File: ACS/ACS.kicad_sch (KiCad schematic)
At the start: 9 parts, among them J1 Screw_Terminal_01x02, Q1 IRLB8721PBF, U1 Teensy4.1

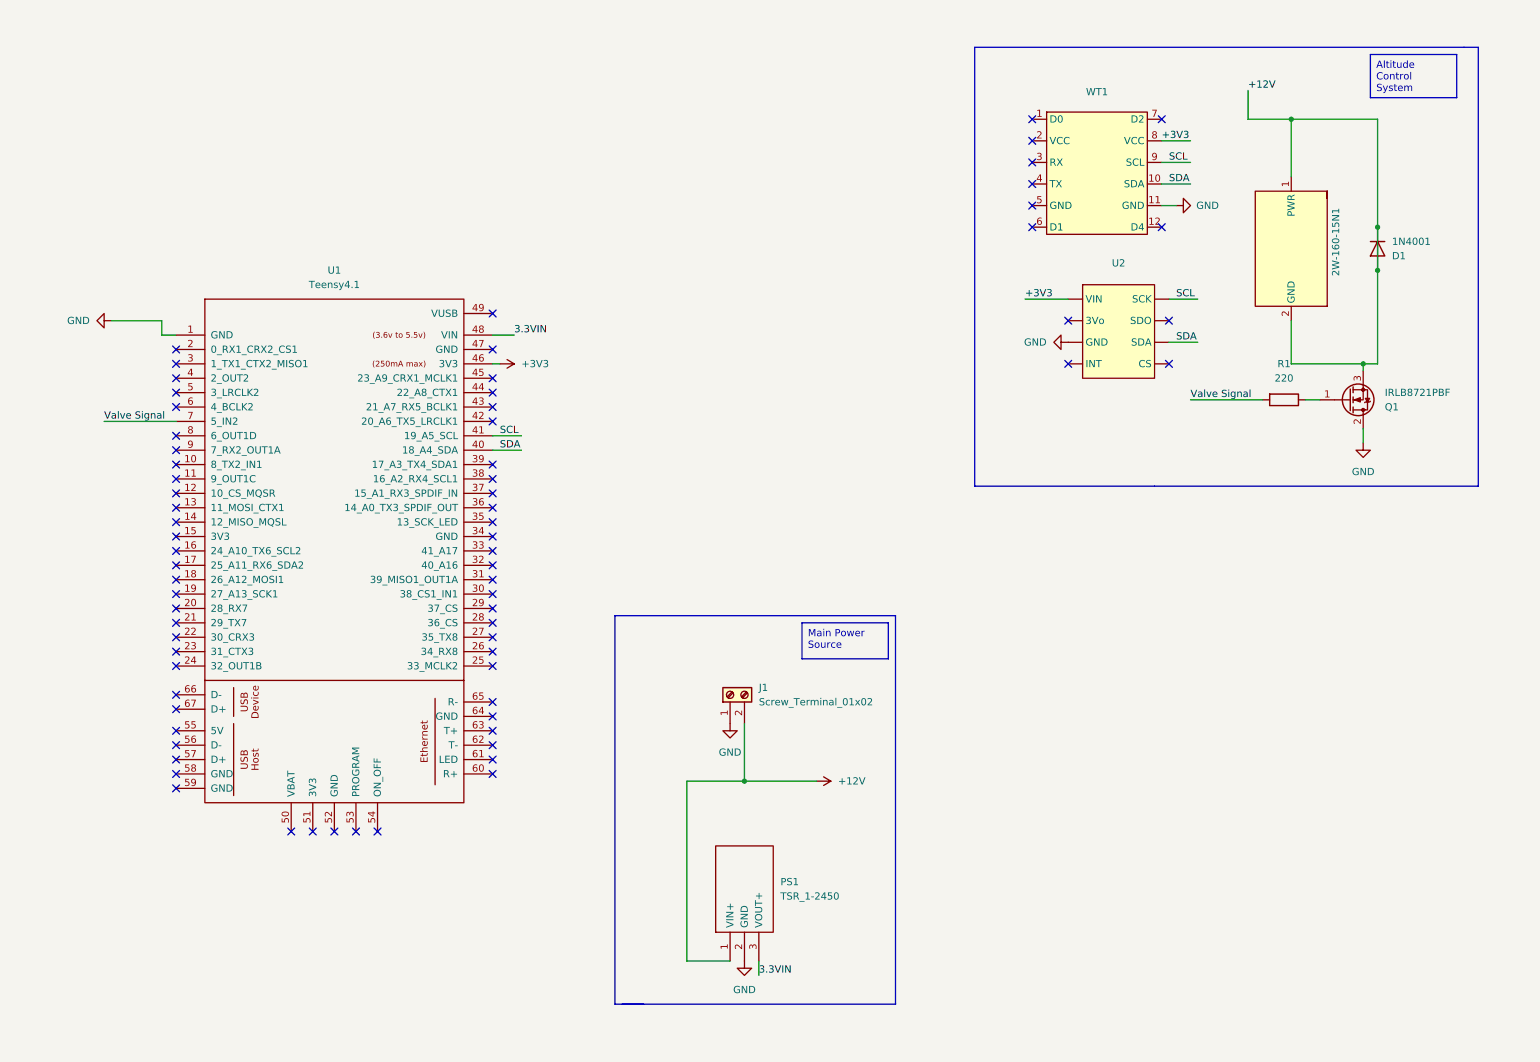
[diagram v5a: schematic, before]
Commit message: Add Switch and Heating Pad
Added wiring for switch and heating pad for ACS. Fix wiring schematic IRLB8721 for solenoid control
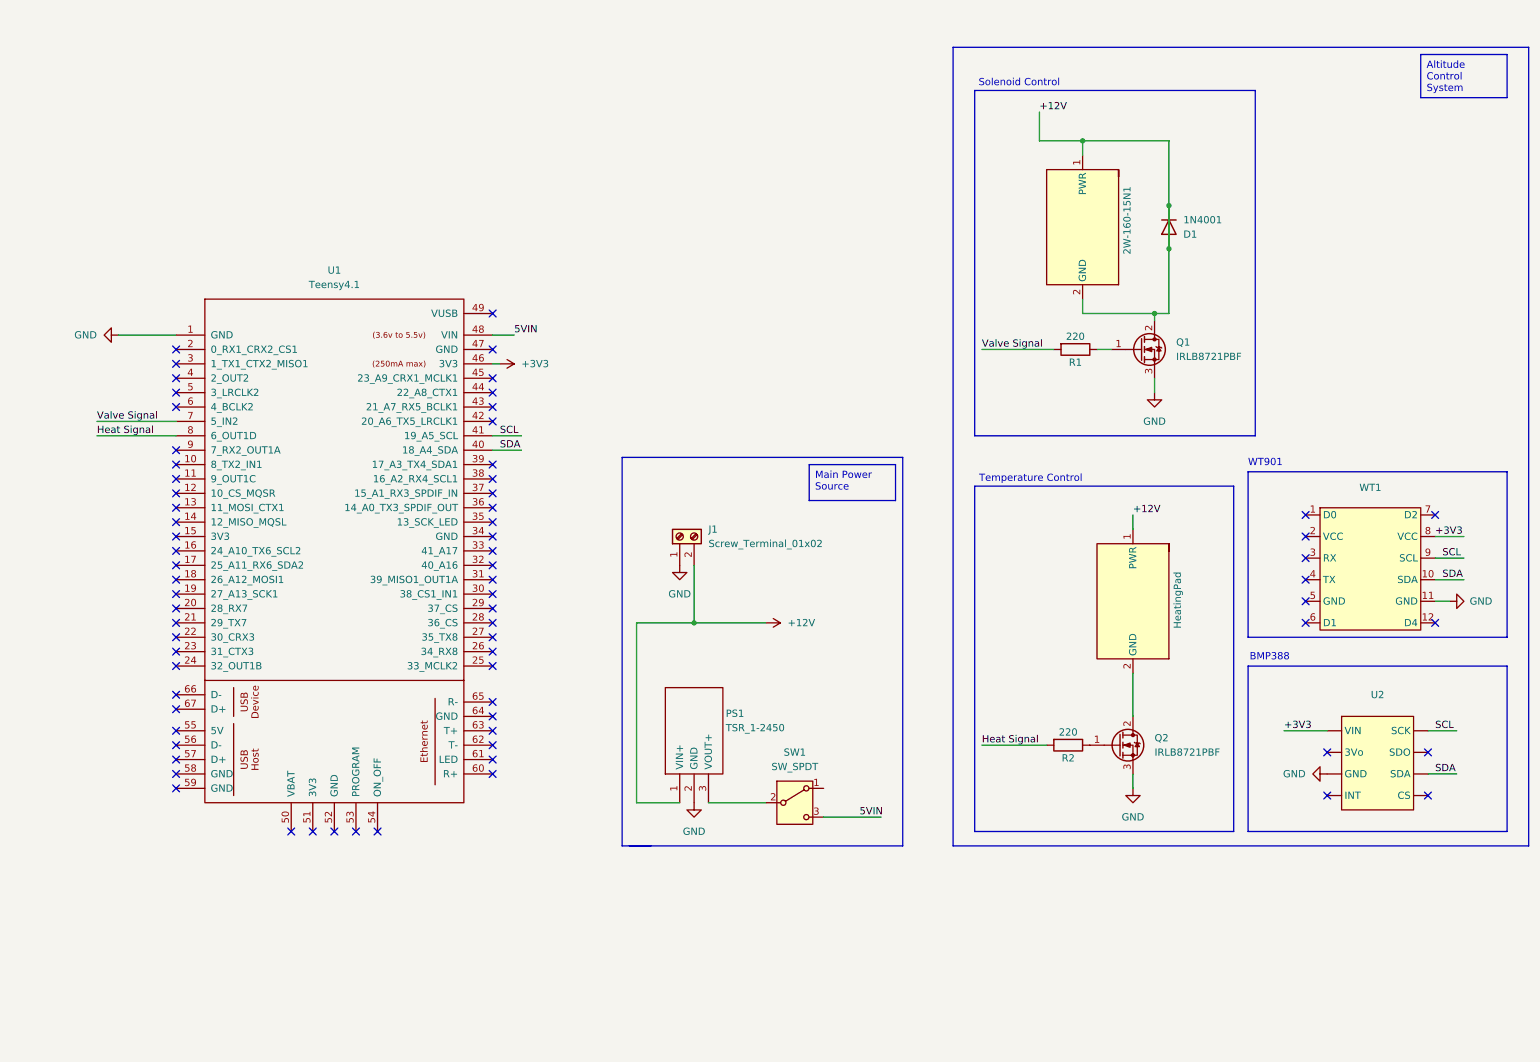
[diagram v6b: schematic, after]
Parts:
- added HeatingPad: ~, TerminalBlock_RND:TerminalBlock_RND_205-00276_1x02_P5.00mm_Vertical, symbol GRS_Valve:2W-160-15
- added Q2: IRLB8721PBF, Package_TO_SOT_THT:TO-220-3_Vertical, symbol Transistor_FET:IRLB8721PBF
- added R2: 220, symbol Device:R
- added SW1: SW_SPDT, symbol Switch:SW_SPDT
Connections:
- net +12V: now also Q1.2 (D), HeatingPad.1 (PWR); no longer Q1.3 (S)
- net GND: now also Q1.3 (S), Q2.3 (S); no longer Q1.2 (D)
- net Heat Signal: now reaches U1.8 (6_OUT1D)
- net Heat Signal: now also R2.2
- net 3.3VIN: no longer names the net of PS1.3 (VOUT+)
- net 3.3VIN: now also SW1.2 (B); no longer U1.48 (VIN)
- new net: HeatingPad.2 (GND), Q2.2 (D)
- new net: Q2.1 (G), R2.1
- new net 5VIN: SW1.3 (C), U1.48 (VIN)
- no-connect marks 73 -> 72
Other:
- note added: "BMP388"
- note added: "Solenoid Control"
- note added: "Temperature Control"
- note added: "WT901"
- moved on the sheet: 2W-160-15N1, D1, J1, PS1, Q1, R1, U2, WT1

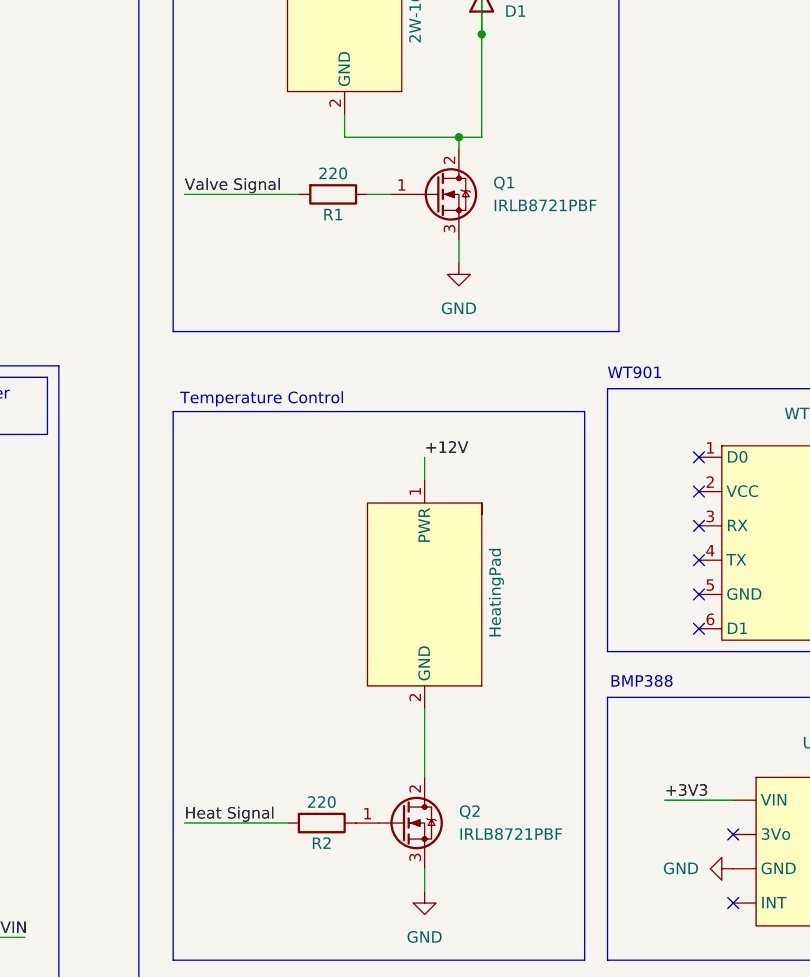
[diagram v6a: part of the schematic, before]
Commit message: added resistor footprints
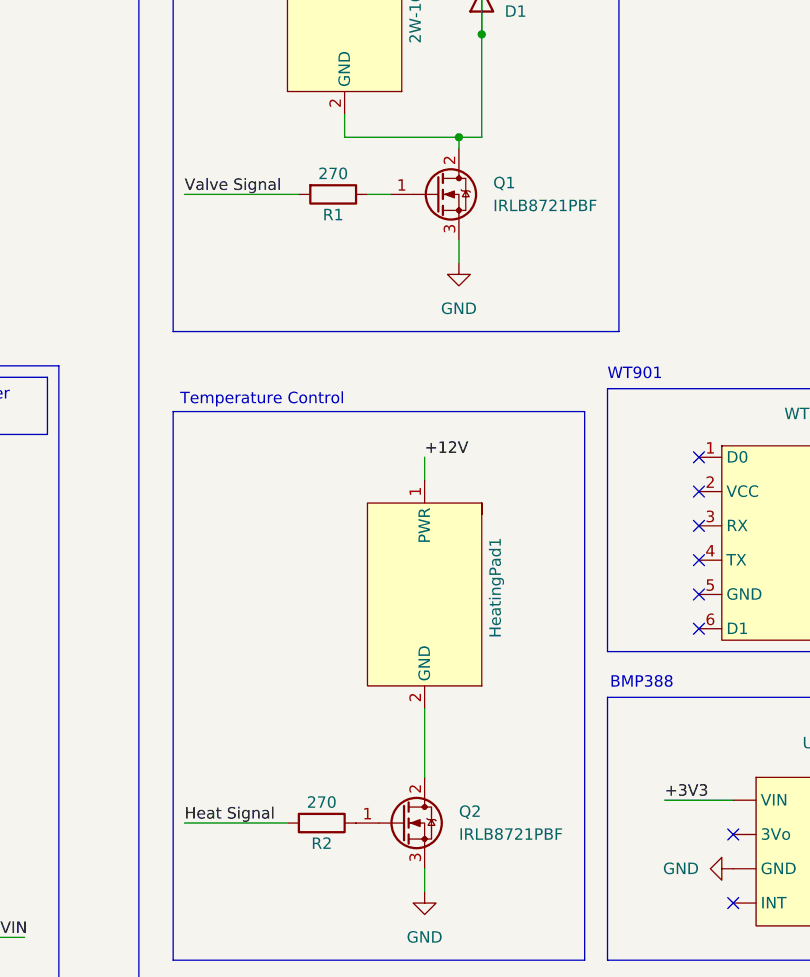
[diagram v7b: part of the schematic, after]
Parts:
- R1, R2: value 220 -> 270; footprint (none) -> Capacitor_THT:CP_Axial_L10.0mm_D4.5mm_P15.00mm_Horizontal
- renumbered HeatingPad to HeatingPad1
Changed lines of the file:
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@@
 		(on_board yes)
 		(dnp no)
-		(property "Reference" "HeatingPad"
+		(property "Reference" "HeatingPad1"
 			(at 217.424 122.936 0)
 			(effects
@@
 			(project "ACS"
 				(path "/da212a0e-0325-4de6-8fc7-5f35040c02c9"
-					(reference "HeatingPad")
+					(reference "HeatingPad1")
 					(unit 1)
 				)
@@
 			)
 		)
-		(property "Value" "220"
+		(property "Value" "270"
 			(at 199.39 71.374 90)
 			(effects
@@
 			)
 		)
-		(property "Footprint" ""
+		(property "Footprint" "Capacitor_THT:CP_Axial_L10.0mm_D4.5mm_P15.00mm_Horizontal"
 			(at 199.39 71.882 90)
 			(effects
@@
 			)
 		)
-		(property "Value" "220"
+		(property "Value" "270"
 			(at 198.12 141.224 90)
 			(effects
@@
 			)
 		)
-		(property "Footprint" ""
+		(property "Footprint" "Capacitor_THT:CP_Axial_L10.0mm_D4.5mm_P15.00mm_Horizontal"
 			(at 198.12 141.732 90)
 			(effects
@@
 		)
 		(instances
-			(project ""
+			(project "ACS"
 				(path "/da212a0e-0325-4de6-8fc7-5f35040c02c9"
 					(reference "SW1")

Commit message: Assigned footprint to U2
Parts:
- U2: footprint (none) -> Connector_PinSocket_2.54mm:PinSocket_1x08_P2.54mm_Vertical
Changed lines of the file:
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@@
 			)
 		)
-		(property "Footprint" ""
+		(property "Footprint" "Connector_PinSocket_2.54mm:PinSocket_1x08_P2.54mm_Vertical"
 			(at 252.73 137.16 0)
 			(effects
